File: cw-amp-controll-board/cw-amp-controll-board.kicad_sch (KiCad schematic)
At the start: 20 parts

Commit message: added i2c port extensions to controll board
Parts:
- removed C? (x2): 100nF, Capacitor_SMD:C_0805_2012Metric_Pad1.18x1.45mm_HandSolder, symbol Device:C
- removed SW? (x2): SW_Push, symbol Switch:SW_Push
- added C? (x2): 100nF, Capacitor_SMD:C_0805_2012Metric_Pad1.18x1.45mm_HandSolder, symbol Device:C
- added Q? (x4): BC850, Package_TO_SOT_SMD:SOT-23, symbol Transistor_BJT:BC850
- added R? (x2): 10k, Resistor_SMD:R_0805_2012Metric_Pad1.20x1.40mm_HandSolder, symbol Device:R
- added R?: 33k, Resistor_SMD:R_0805_2012Metric_Pad1.20x1.40mm_HandSolder, symbol Device:R
- added R?: 51k, Resistor_SMD:R_0805_2012Metric_Pad1.20x1.40mm_HandSolder, symbol Device:R
- added R?: 9k1, Resistor_SMD:R_0805_2012Metric_Pad1.20x1.40mm_HandSolder, symbol Device:R
- added U?: PCF8574, symbol Interface_Expansion:PCF8574
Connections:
- net +3V3: now also U?.1 (A0), U?.16 (VDD), C?.1, C?.1, R?.1, R?.1, U?.16 (VDD)
- net AMP-GAIN0: now also U?.6 (P2)
- net AMP-GAIN1: now also U?.7 (P3)
- net AMP-ShutDown: now also U?.4 (P0)
- net BT-KEY: now also Q?.3 (C), Q?.3 (C), Q?.3 (C), Q?.3 (C)
- net BT-MUTE: now also U?.9 (P4)
- net GNDD: now also U?.2 (A1), U?.3 (A2), U?.8 (VSS), C?.2, C?.2, Q?.2 (E), R?.2, R?.2, R?.2, U?.1 (A0), U?.2 (A1), U?.3 (A2), U?.8 (VSS)
- net SCL: now also U?.14 (SCL), U?.14 (SCL)
- net SDA: now also U?.15 (SDA), U?.15 (SDA)
- net SELECT-Analog: now also U?.9 (P4)
- net SELECT-BT: now also U?.10 (P5)
- net ~{AMP-Mute}: now also U?.5 (P1)
- net LED-ANALOG-INT: now reaches U?.10 (P5)
- net LED-ANALOG-EXT: now reaches U?.11 (P6)
- net LED-BT: now reaches U?.12 (P7)
- net I2CP2-~{INT}: now reaches U?.13 (~{INT})
- net I2CP2-~{INT}: now also R?.2
- net BT-PAUSE: now reaches U?.4 (P0)
- net BT-PAUSE: now also Q?.1 (B)
- net BT-NEXT: now reaches U?.5 (P1)
- net BT-NEXT: now also Q?.1 (B)
- net BT-PREV: now reaches U?.6 (P2)
- net BT-PREV: now also Q?.1 (B)
- net BT-ON-OFF: now reaches U?.7 (P3)
- net BT-ON-OFF: now also Q?.1 (B)
- new net BT-KEY-NEXT: Q?.2 (E), R?.1
- new net BT-KEY-PAUSE: Q?.2 (E), R?.1
- new net BT-KEY-PREV: Q?.2 (E), R?.1
- new net I2CP1-~{INT}: R?.2, U?.13 (~{INT})
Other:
- note added: "ESP32-C3"
- note added: "I2C Port 1"
- note added: "I2C Port 2"
- note added: "READ: 0x41 WRITE: 0x40"
- note added: "READ: 0x43 WRITE: 0x42"
- note added: "Rotary Encoder"
- note removed: "Auto prpgram"
- note removed: "Manual prpgram"
- moved on the sheet: C?, J?, R?, SW?, U?

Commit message: Added bluetooth vcc filter, moved i2c pullups to controll board, added touch controller
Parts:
- added C?: 1µF, Capacitor_SMD:C_0805_2012Metric_Pad1.18x1.45mm_HandSolder, symbol Device:C
- added J?: Conn_02x05_Odd_Even, symbol Connector_Generic:Conn_02x05_Odd_Even
- added R? (x4): 4k7, Resistor_SMD:R_0805_2012Metric_Pad1.20x1.40mm_HandSolder, symbol Device:R
- added R? (x2): 10k, Resistor_SMD:R_0805_2012Metric_Pad1.20x1.40mm_HandSolder, symbol Device:R
- added R?: 39k, Resistor_SMD:R_0805_2012Metric_Pad1.20x1.40mm_HandSolder, symbol Device:R
- added R?: 9k1, Resistor_SMD:R_0805_2012Metric_Pad1.20x1.40mm_HandSolder, symbol Device:R
- added U?: AT42QT2120-CommsMode, Package_SO:SOIC-20W_7.5x12.8mm_P1.27mm, symbol office amp:AT42QT2120-CommsMode
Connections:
- net +3V3: now also C?.2, J?.9 (Pin_9), R?.1, R?.1, R?.1, U?.10 (VSS), U?.12 (MODE), U?.14 (~{RESET})
- net GNDD: now also C?.1, J?.10 (Pin_10), U?.11 (VDD)
- net LED-ANALOG-EXT: now also J?.3 (Pin_3)
- net LED-ANALOG-INT: now also J?.5 (Pin_5)
- net LED-BT: now also J?.1 (Pin_1)
- net SCL: now also U?.3 (GPIO4/ADC1_CH4), R?.2, U?.16 (SCL)
- net SDA: now also U?.4 (GPIO5/ADC2_CH0), R?.2, U?.13 (SDA)
- new net TOUCH-KEY-0-POWER: R?.2, U?.9 (KEY0)
- new net TOUCH-KEY-1-ANALOG-EXT: R?.2, U?.8 (KEY1)
- new net TOUCH-KEY-4-BT: R?.2, U?.6 (KEY3/GPO1)
- new net TOUCH-KEY-ANALOG-EXT: J?.4 (Pin_4), R?.1
- new net TOUCH-KEY-ANALOG-INT: J?.6 (Pin_6), R?.1
- new net TOUCH-KEY-BT: J?.8 (Pin_8), R?.1
- new net TOUCH-KEY-POWER: J?.2 (Pin_2), R?.1
- new net TOUCH-KEY2-ANALOG-INT: R?.2, U?.7 (KEY2/GPO0)
- new net ~{TOUCH-INT}: R?.2, U?.17 (~{CHANGE})
- new net ~{TOUCH-INT}-PULL-UP: R?.1, R?.2
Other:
- added sheet ESP-AUDIO (ESP-AUDIO.kicad_sch)
- note added: "I2C Touch-Controller"
- note added: "Touch Pannel Connection"
- note removed: "AT42QT2120 Touch IC einbauen"
- moved on the sheet: C?, R?

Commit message: finisched ESP32 Audio, started placement
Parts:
- added R21, R22, R23, R24, R25, R26, R27, R28: 10k, Resistor_SMD:R_0805_2012Metric_Pad1.20x1.40mm_HandSolder, symbol Device:R
- J2: renamed from J?; value Conn_01x06 -> (none)
- J3: renamed from J?; value Conn_02x05_Odd_Even -> (none)
- SW1: renamed from SW?; value RotaryEncoder -> (none)
- gave numbers to parts that had none: 36
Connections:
- net GNDD: now also R22.1, R24.1, R26.1, R28.1
- net DIN: now reaches U3.10 (GPIO10)
- net LRCLK: now reaches U3.15 (GPIO3/ADC1_CH3)
- net BCK: now reaches U3.17 (GPIO1/ADC1_CH1/XTAL_32K_N)
- net SCK: now reaches U3.18 (GPIO0/ADC1_CH0/XTAL_32K_P)
- net BT-NEXT renamed BT-NEXT-P1
- net BT-NEXT-P1: now also R23.1; no longer Q2.1 (B)
- net BT-ON-OFF renamed BT-ON-OFF-P3
- net BT-ON-OFF-P3: now also R27.1; no longer Q4.1 (B)
- net BT-PAUSE renamed BT-PAUSE-P0
- net BT-PAUSE-P0: now also R21.1; no longer Q1.1 (B)
- net BT-PREV renamed BT-PREV-P2
- net BT-PREV-P2: now also R25.1; no longer Q3.1 (B)
- new net BT-NEXT-Q2: Q2.1 (B), R23.2, R24.2
- new net BT-ON-OFF-Q4: Q4.1 (B), R27.2, R28.2
- new net BT-PAUSE-Q1: Q1.1 (B), R21.2, R22.2
- new net BT-PREV-Q3: Q3.1 (B), R25.2, R26.2
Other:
- moved on the sheet: C6, Q1, Q2, Q3, Q4, R10, R11, R15, R16, R17, R18, R7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

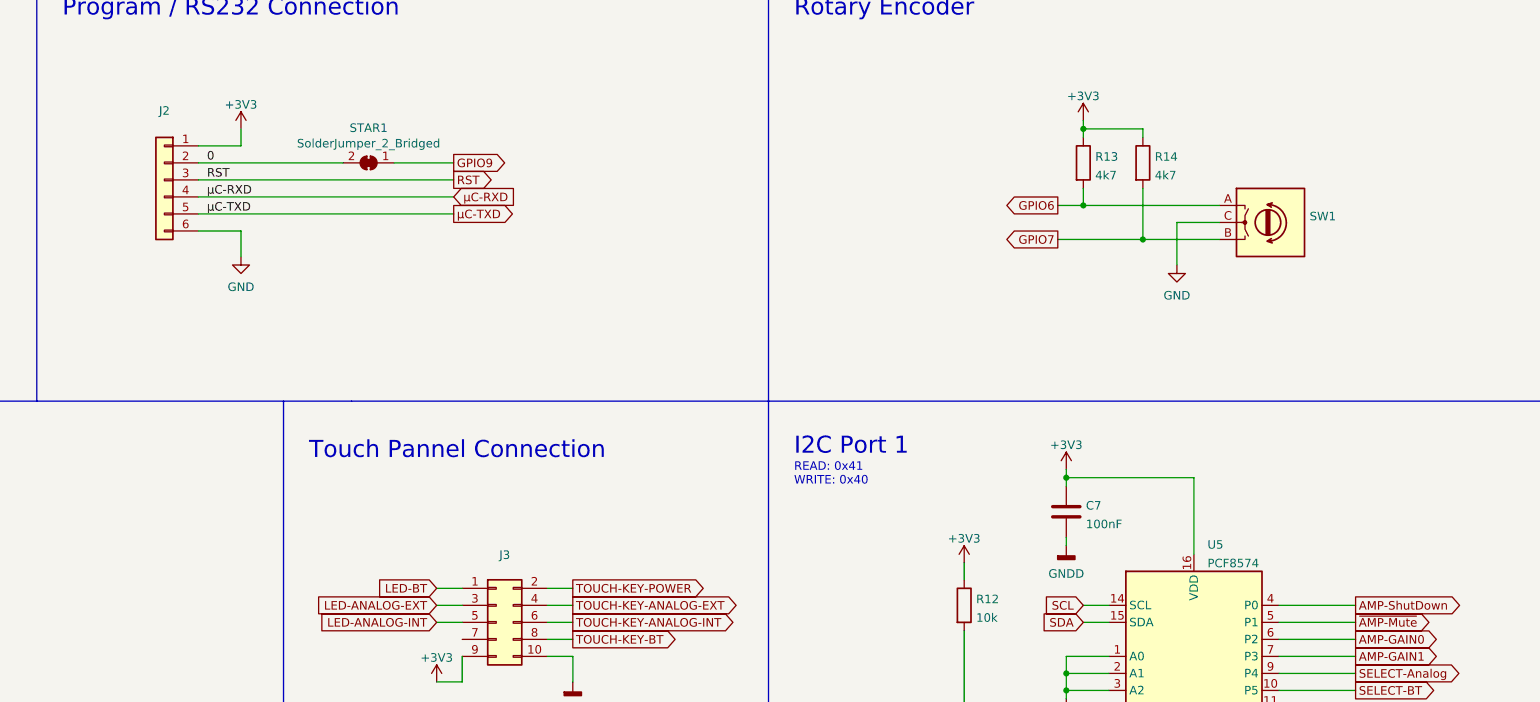
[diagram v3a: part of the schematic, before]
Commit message: First placement controll board
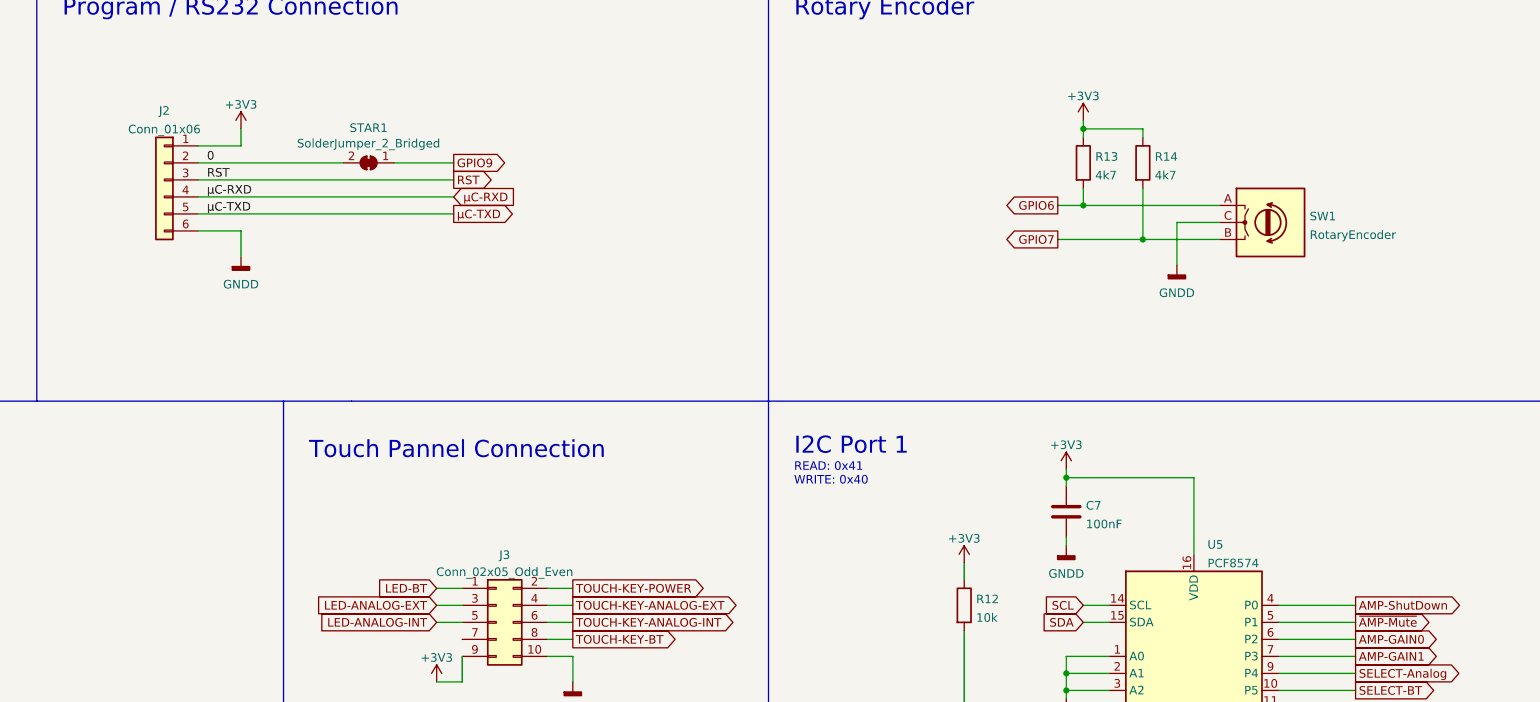
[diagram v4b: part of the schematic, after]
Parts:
- J2: value (none) -> Conn_01x06; footprint (none) -> Connector_PinHeader_2.54mm:PinHeader_1x06_P2.54mm_Horizontal
- J3: value (none) -> Conn_02x05_Odd_Even; footprint (none) -> Connector_IDC:IDC-Header_2x05_P2.54mm_Vertical
- SW1: value (none) -> RotaryEncoder; footprint (none) -> office_amp:ALPS_STEC11B
- U2, U5: footprint (none) -> Package_SO:SOIC-16W_7.5x10.3mm_P1.27mm
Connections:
- net GND is gone; now on net GNDD: J2.6 (Pin_6), SW1.C
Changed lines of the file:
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@@
     (in_bom yes) (on_board yes) (fields_autoplaced)
     (property "Reference" "J3" (id 0) (at 251.46 99.1702 0))
-    (property "Value" "" (id 1) (at 251.46 101.7071 0))
-    (property "Footprint" "" (id 2) (at 250.19 109.22 0)
+    (property "Value" "Conn_02x05_Odd_Even" (id 1) (at 251.46 101.7071 0))
+    (property "Footprint" "Connector_IDC:IDC-Header_2x05_P2.54mm_Vertical" (id 2) (at 250.19 109.22 0)
       (effects (font (size 1.27 1.27)) hide)
     )
@@
     (in_bom yes) (on_board yes) (fields_autoplaced)
     (property "Reference" "J2" (id 0) (at 200.66 32.8635 0))
-    (property "Value" "" (id 1) (at 200.66 35.6386 0))
-    (property "Footprint" "" (id 2) (at 200.66 43.18 0)
+    (property "Value" "Conn_01x06" (id 1) (at 200.66 35.6386 0))
+    (property "Footprint" "Connector_PinHeader_2.54mm:PinHeader_1x06_P2.54mm_Horizontal" (id 2) (at 200.66 43.18 0)
       (effects (font (size 1.27 1.27)) hide)
     )
@@
       (effects (font (size 1.27 1.27)) (justify left))
     )
-    (property "Value" "" (id 1) (at 371.602 51.3966 0)
-      (effects (font (size 1.27 1.27)) (justify left))
-    )
-    (property "Footprint" "" (id 2) (at 361.95 45.466 0)
+    (property "Value" "RotaryEncoder" (id 1) (at 371.602 51.3966 0)
+      (effects (font (size 1.27 1.27)) (justify left))
+    )
+    (property "Footprint" "office_amp:ALPS_STEC11B" (id 2) (at 361.95 45.466 0)
       (effects (font (size 1.27 1.27)) hide)
     )
@@
       (effects (font (size 1.27 1.27)) (justify left))
     )
-    (property "Footprint" "" (id 2) (at 354.33 116.84 0)
+    (property "Footprint" "Package_SO:SOIC-16W_7.5x10.3mm_P1.27mm" (id 2) (at 354.33 116.84 0)
       (effects (font (size 1.27 1.27)) hide)
     )
@@
       (effects (font (size 1.27 1.27)) (justify left))
     )
-    (property "Footprint" "" (id 2) (at 60.96 255.27 0)
+    (property "Footprint" "Package_SO:SOIC-16W_7.5x10.3mm_P1.27mm" (id 2) (at 60.96 255.27 0)
       (effects (font (size 1.27 1.27)) hide)
     )
@@
     (pin "2")
   )
-  (symbol (lib_id "power:GND") (at 212.09 54.61 0) (unit 1)
-    (in_bom yes) (on_board yes) (fields_autoplaced)
-    (property "Reference" "#PWR030" (id 0) (at 212.09 60.96 0)
-      (effects (font (size 1.27 1.27)) hide)
-    )
-    (property "Value" "GND" (id 1) (at 212.09 59.1725 0))
-    (property "Footprint" "" (id 2) (at 212.09 54.61 0)
-      (effects (font (size 1.27 1.27)) hide)
-    )
-    (property "Datasheet" "" (id 3) (at 212.09 54.61 0)
-      (effects (font (size 1.27 1.27)) hide)
-    )
-    (pin "1")
-  )
   (symbol (lib_id "Device:R") (at 52.07 114.3 0) (unit 1)
     (in_bom yes) (on_board yes) (fields_autoplaced)
@@
     (pin "2")
     (pin "3")
-  )
-  (symbol (lib_id "power:GND") (at 351.79 55.88 0) (unit 1)
-    (in_bom yes) (on_board yes) (fields_autoplaced)
-    (property "Reference" "#PWR042" (id 0) (at 351.79 62.23 0)
-      (effects (font (size 1.27 1.27)) hide)
-    )
-    (property "Value" "GND" (id 1) (at 351.79 60.4425 0))
-    (property "Footprint" "" (id 2) (at 351.79 55.88 0)
-      (effects (font (size 1.27 1.27)) hide)
-    )
-    (property "Datasheet" "" (id 3) (at 351.79 55.88 0)
-      (effects (font (size 1.27 1.27)) hide)
-    )
-    (pin "1")
   )
   (symbol (lib_id "power:+3V3") (at 25.4 238.76 0) (unit 1)
@@
     (pin "2")
   )
+  (symbol (lib_id "power:GNDD") (at 212.09 54.61 0) (unit 1)
+    (in_bom yes) (on_board yes) (fields_autoplaced)
+    (property "Reference" "#PWR?" (id 0) (at 212.09 60.96 0)
+      (effects (font (size 1.27 1.27)) hide)
+    )
+    (property "Value" "GNDD" (id 1) (at 212.09 58.7915 0))
+    (property "Footprint" "" (id 2) (at 212.09 54.61 0)
+      (effects (font (size 1.27 1.27)) hide)
+    )
+    (property "Datasheet" "" (id 3) (at 212.09 54.61 0)
+      (effects (font (size 1.27 1.27)) hide)
+    )
+    (pin "1")
+  )
   (symbol (lib_id "Device:R") (at 172.72 260.35 0) (unit 1)
     (in_bom yes) (on_board yes) (fields_autoplaced)
@@
     )
     (property "Datasheet" "" (id 3) (at 335.28 97.79 0)
+      (effects (font (size 1.27 1.27)) hide)
+    )
+    (pin "1")
+  )
+  (symbol (lib_id "power:GNDD") (at 351.79 55.88 0) (unit 1)
+    (in_bom yes) (on_board yes) (fields_autoplaced)
+    (property "Reference" "#PWR?" (id 0) (at 351.79 62.23 0)
+      (effects (font (size 1.27 1.27)) hide)
+    )
+    (property "Value" "GNDD" (id 1) (at 351.79 60.0615 0))
+    (property "Footprint" "" (id 2) (at 351.79 55.88 0)
+      (effects (font (size 1.27 1.27)) hide)
+    )
+    (property "Datasheet" "" (id 3) (at 351.79 55.88 0)
       (effects (font (size 1.27 1.27)) hide)
     )
@@
       (reference "#PWR029") (unit 1) (value "+3V3") (footprint "")
     )
-    (path "/849b88c0-f398-498d-909f-d632de3d465d"
-      (reference "#PWR030") (unit 1) (value "GND") (footprint "")
-    )
     (path "/5c9c74d9-29fc-4f8d-aebc-9ea56399e608"
       (reference "#PWR031") (unit 1) (value "+3V3") (footprint "")
@@
       (reference "#PWR041") (unit 1) (value "+3V3") (footprint "")
     )
-    (path "/96151c8c-4f1b-442d-807f-05f9773637a0"
-      (reference "#PWR042") (unit 1) (value "GND") (footprint "")
-    )
     (path "/000bf9e0-d9fd-4ff6-8ed1-98d540c4d2c6"
       (reference "#PWR043") (unit 1) (value "GNDD") (footprint "")
@@
       (reference "#PWR0104") (unit 1) (value "GNDD") (footprint "")
     )
+    (path "/a7beda29-64db-42f0-bcb0-f16f1db3caf3"
+      (reference "#PWR?") (unit 1) (value "GNDD") (footprint "")
+    )
+    (path "/c42ae11f-3078-4272-8158-475a1544e2a0"
+      (reference "#PWR?") (unit 1) (value "GNDD") (footprint "")
+    )
     (path "/c69b3723-8151-4cdf-9090-67c835ef0944"

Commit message: routing controller
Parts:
- added FID1, FID2, FID3: Fiducial, Fiducial:Fiducial_1.5mm_Mask3mm, symbol Mechanical:Fiducial
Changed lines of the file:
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@@
   (symbol (lib_id "power:GNDD") (at 212.09 54.61 0) (unit 1)
     (in_bom yes) (on_board yes) (fields_autoplaced)
-    (property "Reference" "#PWR?" (id 0) (at 212.09 60.96 0)
+    (property "Reference" "#PWR0105" (id 0) (at 212.09 60.96 0)
       (effects (font (size 1.27 1.27)) hide)
     )
@@
     (pin "1")
   )
+  (symbol (lib_id "Mechanical:Fiducial") (at 313.69 248.92 0) (unit 1)
+    (in_bom yes) (on_board yes) (fields_autoplaced)
+    (property "Reference" "FID2" (id 0) (at 315.849 248.0115 0)
+      (effects (font (size 1.27 1.27)) (justify left))
+    )
+    (property "Value" "Fiducial" (id 1) (at 315.849 250.7866 0)
+      (effects (font (size 1.27 1.27)) (justify left))
+    )
+    (property "Footprint" "Fiducial:Fiducial_1.5mm_Mask3mm" (id 2) (at 313.69 248.92 0)
+      (effects (font (size 1.27 1.27)) hide)
+    )
+    (property "Datasheet" "~" (id 3) (at 313.69 248.92 0)
+      (effects (font (size 1.27 1.27)) hide)
+    )
+  )
   (symbol (lib_id "power:GNDD") (at 351.79 55.88 0) (unit 1)
     (in_bom yes) (on_board yes) (fields_autoplaced)
-    (property "Reference" "#PWR?" (id 0) (at 351.79 62.23 0)
+    (property "Reference" "#PWR0106" (id 0) (at 351.79 62.23 0)
       (effects (font (size 1.27 1.27)) hide)
     )
@@
     (pin "1")
   )
+  (symbol (lib_id "Mechanical:Fiducial") (at 326.39 248.92 0) (unit 1)
+    (in_bom yes) (on_board yes) (fields_autoplaced)
+    (property "Reference" "FID3" (id 0) (at 328.549 248.0115 0)
+      (effects (font (size 1.27 1.27)) (justify left))
+    )
+    (property "Value" "Fiducial" (id 1) (at 328.549 250.7866 0)
+      (effects (font (size 1.27 1.27)) (justify left))
+    )
+    (property "Footprint" "Fiducial:Fiducial_1.5mm_Mask3mm" (id 2) (at 326.39 248.92 0)
+      (effects (font (size 1.27 1.27)) hide)
+    )
+    (property "Datasheet" "~" (id 3) (at 326.39 248.92 0)
+      (effects (font (size 1.27 1.27)) hide)
+    )
+  )
   (symbol (lib_id "Device:C") (at 85.09 167.64 0) (unit 1)
     (in_bom yes) (on_board yes) (fields_autoplaced)
@@
     )
     (pin "1")
+  )
+  (symbol (lib_id "Mechanical:Fiducial") (at 300.99 248.92 0) (unit 1)
+    (in_bom yes) (on_board yes) (fields_autoplaced)
+    (property "Reference" "FID1" (id 0) (at 303.149 248.0115 0)
+      (effects (font (size 1.27 1.27)) (justify left))
+    )
+    (property "Value" "Fiducial" (id 1) (at 303.149 250.7866 0)
+      (effects (font (size 1.27 1.27)) (justify left))
+    )
+    (property "Footprint" "Fiducial:Fiducial_1.5mm_Mask3mm" (id 2) (at 300.99 248.92 0)
+      (effects (font (size 1.27 1.27)) hide)
+    )
+    (property "Datasheet" "~" (id 3) (at 300.99 248.92 0)
+      (effects (font (size 1.27 1.27)) hide)
+    )
   )
   (symbol (lib_id "Device:R") (at 360.68 194.31 270) (unit 1)
@@
     )
     (path "/a7beda29-64db-42f0-bcb0-f16f1db3caf3"
-      (reference "#PWR?") (unit 1) (value "GNDD") (footprint "")
+      (reference "#PWR0105") (unit 1) (value "GNDD") (footprint "")
     )
     (path "/c42ae11f-3078-4272-8158-475a1544e2a0"
-      (reference "#PWR?") (unit 1) (value "GNDD") (footprint "")
+      (reference "#PWR0106") (unit 1) (value "GNDD") (footprint "")
     )
     (path "/c69b3723-8151-4cdf-9090-67c835ef0944"
@@
       (reference "C18") (unit 1) (value "1µF") (footprint "Capacitor_SMD:C_0805_2012Metric_Pad1.18x1.45mm_HandSolder")
     )
+    (path "/ec6426f2-070e-416b-bfdd-53787a156564"
+      (reference "FID1") (unit 1) (value "Fiducial") (footprint "Fiducial:Fiducial_1.5mm_Mask3mm")
+    )
+    (path "/c421ef33-a111-44e5-bce9-43a46ebbb387"
+      (reference "FID2") (unit 1) (value "Fiducial") (footprint "Fiducial:Fiducial_1.5mm_Mask3mm")
+    )
+    (path "/df7c9b52-2269-46a0-9a95-b0ef1f46dcb2"
+      (reference "FID3") (unit 1) (value "Fiducial") (footprint "Fiducial:Fiducial_1.5mm_Mask3mm")
+    )
     (path "/3c1859dc-33d6-48ca-97a8-d652f7b04c48"
